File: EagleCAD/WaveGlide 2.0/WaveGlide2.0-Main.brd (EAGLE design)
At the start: 100 x 100 mm, 7 parts, among them K1 AQY21SOP, K2 MS-20-310-HN, U1 ATMEGA328P_TQFP, U2 BMP180, U3 MPXV7002, X1 22-23-2111

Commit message: Updated docs and part additions
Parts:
- added IC1: TPS77033, texas:SOT23-DBV
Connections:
- net GND: now also IC1.2
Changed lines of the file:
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@@
 <attribute name="OC_NEWARK" value="27C9916" x="15.7" y="94.9" size="1.778" layer="27" display="off"/>
+</element>
+<element name="IC1" library="texas" library_urn="urn:adsk.eagle:library:387" package="SOT23-DBV" value="TPS77033" x="26.5" y="49">
+<attribute name="MF" value="TEXAS INSTRUMENTS" x="26.5" y="49" size="1.778" layer="27" display="off"/>
+<attribute name="MPN" value="TPS77033DBVT" x="26.5" y="49" size="1.778" layer="27" display="off"/>
+<attribute name="OC_FARNELL" value="8461570" x="26.5" y="49" size="1.778" layer="27" display="off"/>
+<attribute name="OC_NEWARK" value="77C1187" x="26.5" y="49" size="1.778" layer="27" display="off"/>
 </element>
 </elements>
@@
 <signal name="GND">
 <contactref element="U2" pad="7"/>
+<contactref element="K2" pad="P$3"/>
+<contactref element="IC1" pad="2"/>
 <contactref element="U3" pad="3"/>
-<contactref element="K2" pad="P$3"/>
-<wire x1="59.482" y1="89.18" x2="11.48" y2="41.97" width="0" layer="19" extent="1-1"/>
-<wire x1="49.4" y1="25.45" x2="59.482" y2="89.18" width="0" layer="19" extent="1-1"/>
+<wire x1="26.5" y1="47.7" x2="59.482" y2="89.18" width="0" layer="19" extent="1-1"/>
+<wire x1="11.48" y1="41.97" x2="26.5" y2="47.7" width="0" layer="19" extent="1-1"/>
+<wire x1="49.4" y1="25.45" x2="26.5" y2="47.7" width="0" layer="19" extent="1-1"/>
 </signal>
 <signal name="VDD">

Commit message: Updated Schematic
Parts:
- removed X1: 22-23-2111, con-molex:22-23-2111
- added C10, C6: 10uF/16V, microbuilder:_0805MP
- added C7, C8: 1.0uF, microbuilder:_0805MP
- added C9: 10uF, microbuilder:_0805MP
- added D4, D5: 1N4148, microbuilder:SOD-323
- added R1: 560k, microbuilder:_0805MP
- added R2: 50, microbuilder:_0805MP
- added U5: UG-2828GDEDF11, microbuilder:FPC_XF2M-3015-1A
- IC1: device texas:SOT23-DBV -> CustomParts:SOT23-DBV
- U1: device SparkFun-IC-Microcontroller:TQFP32-08 -> CustomParts:TQFP32-08
- U2: device SparkFun-Sensors:BMP180 -> CustomParts:BMP180
- moved IC1 56.2 mm to (-5.00, 2.50)
- moved D1 14.0 mm to (19.9, 27.4)
- moved U1 13.5 mm to (13.5, 69.5)
- moved U3 9.61 mm to (42.0, 81.0)
- moved U2 9.54 mm to (9.50, 51.5)
- moved K2 9.43 mm to (40.0, 31.0)
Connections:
- new net 13V: C6.1, U5.P$29
- new net 3V3: C7.1, C9.1, U5.P$27, U5.P$4
- new net N$2: D4.A, R2.1
- new net N$3: C10.1, U5.P$28
- new net N$4: U5.P$5
- new net N$5: D4.C, D5.A
- new net N$6: C8.1
- new net N$7: R1.2, U5.P$9
- new net N$8: R2.2, U5.P$26
- new net OLED_BS0: U5.P$14
- new net OLED_CS: U5.P$12
- new net OLED_DC: U5.P$11
- new net OLED_MOSI: U5.P$18
- new net OLED_RES: U5.P$10
- new net OLED_SCK: U5.P$17
- net GND: now also C10.2, C6.2, C7.2, C8.2, C9.2, D5.C, K2.3, R1.1, U5.P$1, U5.P$13, U5.P$3, U5.P$30; no longer K2.P$3
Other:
- board size 100 x 100 mm -> 79 x 103 mm

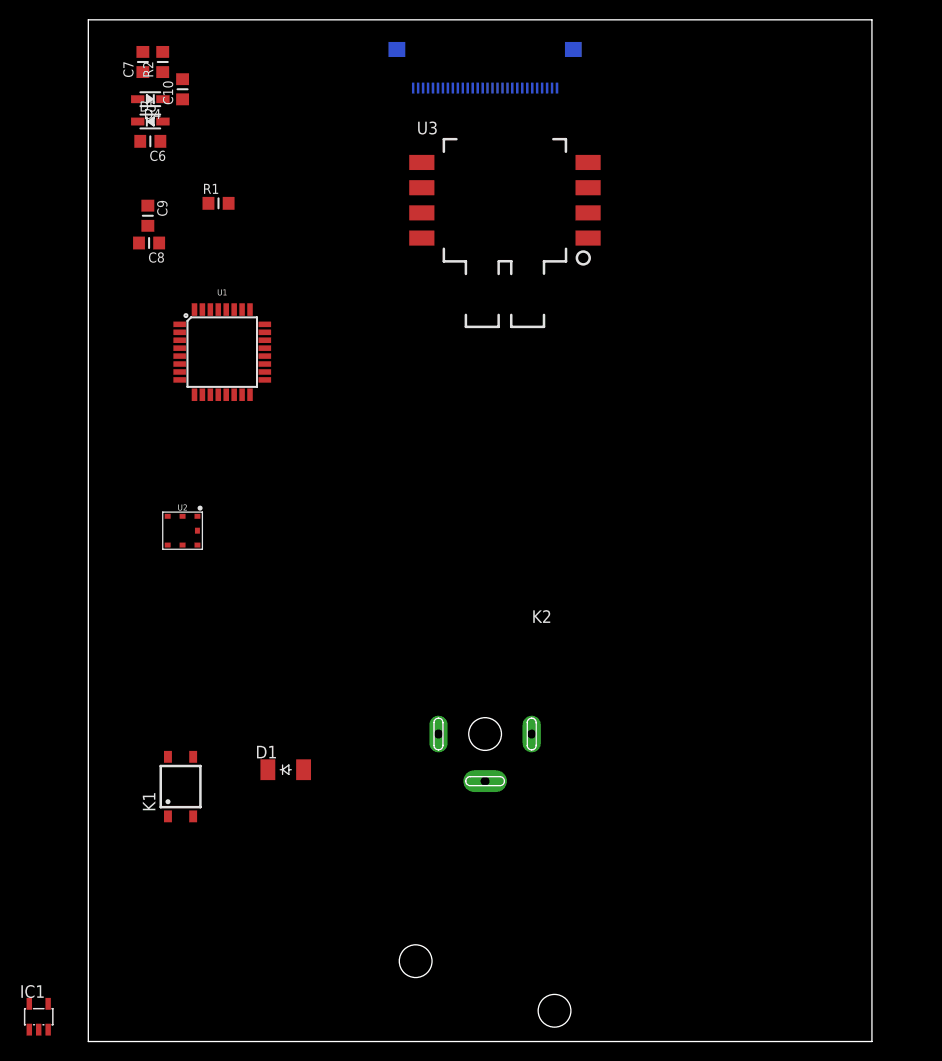
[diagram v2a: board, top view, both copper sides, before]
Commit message: Start generating schematic
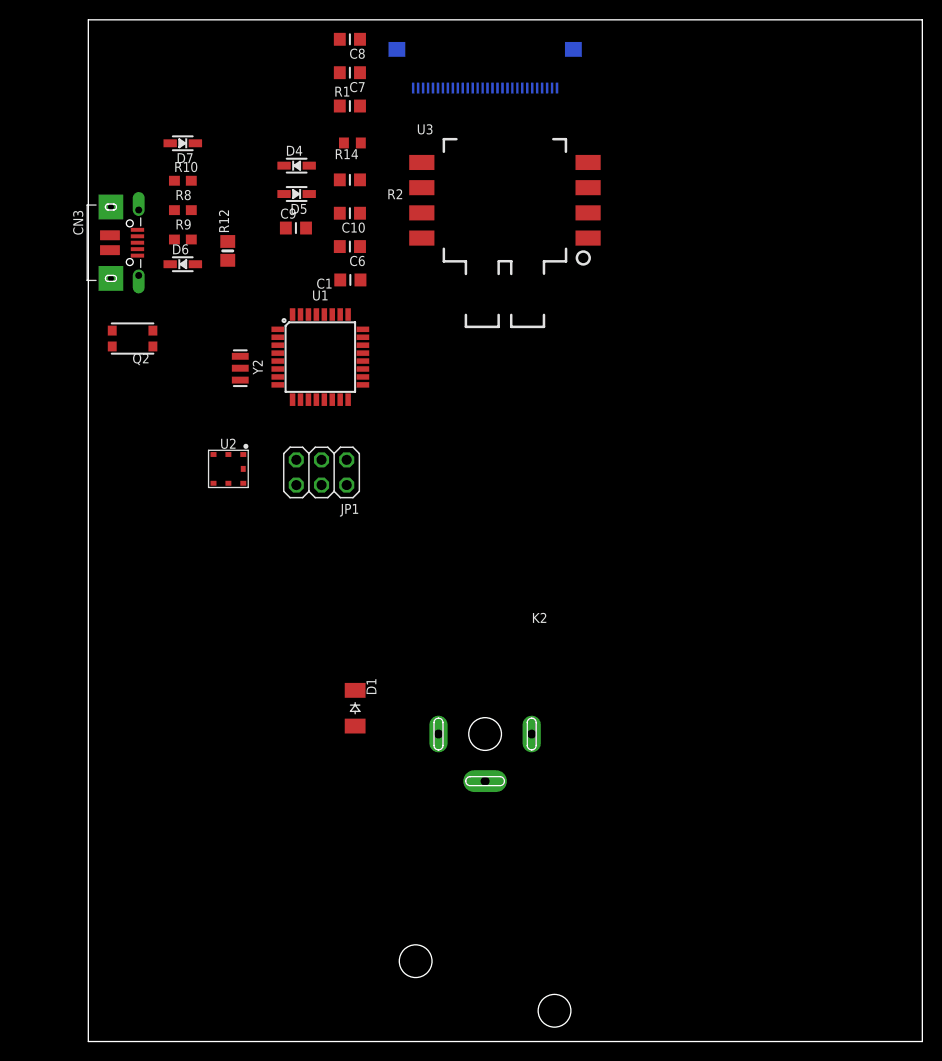
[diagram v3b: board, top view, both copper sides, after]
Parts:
- removed IC1: TPS77033, CustomParts:SOT23-DBV
- removed K1: AQY21SOP, relay:SOP04
- added C1: 0.1uF, microbuilder:_0805MP
- added CN3: 0, microbuilder:4UCONN_20329
- added D6: 3.6v, microbuilder:SOD-323
- added D7: 3.6V, microbuilder:SOD-323
- added JP1: 0, pinhead:2X03
- added Q2: reset, microbuilder:BTN_KMR2_4.6X2.8
- added R10: 1.5K (0603), microbuilder:0603-NO
- added R12: 10K, microbuilder:0805-NO
- added R14: 10k, resistor:R0603
- added R8, R9: 68 (0603), microbuilder:0603-NO
- added Y2: 12MHz, SparkFun:RESONATOR-SMD
- moved C8 28.8 mm to (26.4, 101.0)
- moved C6 22.7 mm to (26.4, 80.1)
- moved R2 22.3 mm to (26.4, 86.9), turned to 180 degrees
- moved C10 21.0 mm to (26.4, 83.5), turned to 180 degrees
- moved C7 20.9 mm to (26.4, 97.7), turned to 180 degrees
- moved R1 16.5 mm to (26.4, 94.3)
- moved D5 16.5 mm to (21.0, 85.4), turned to 180 degrees
- moved D4 16.2 mm to (21.0, 88.3), turned to 0 degrees
- moved C9 15.0 mm to (20.9, 82.0), turned to 0 degrees
- moved U1 9.90 mm to (23.4, 69.0)
- moved D1 9.35 mm to (26.9, 33.6), turned to 270 degrees
- moved U2 7.76 mm to (14.1, 57.7)
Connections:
- net 13V renamed SYS_13V
- net N$3 renamed OLED_VCOMH
- net N$7 renamed OLED_IREF
- net N$8 renamed OLED_VSL
- removed net 3V3: C7.1, C9.1, U5.P$27, U5.P$4
- removed net N$4: U5.P$5
- removed net N$6: C8.1
- removed net OLED_BS0: U5.P$14
- removed net OLED_CS: U5.P$12
- removed net OLED_DC: U5.P$11
- removed net OLED_MOSI: U5.P$18
- removed net OLED_RES: U5.P$10
- removed net OLED_SCK: U5.P$17
- removed net VDD: U2.2
- removed net VDDIO: U2.3
- new net BMP180_3V3: U2.2, U2.3
- new net D+1: CN3.D+, D6.C, R9.1
- new net D-1: CN3.D-, D7.C, R10.1, R8.1
- new net MCU_AREF: C1.1, U1.20
- new net MCU_I2C_SCL: U1.28, U2.5
- new net MCU_I2C_SDA: U1.27, U2.6
- new net MCU_OLED_CS: R14.1, U1.14, U5.P$12
- new net MCU_OLED_DC: U1.12, U5.P$11
- new net MCU_OLED_RES: U1.13, U5.P$10
- new net MCU_PROG/OLED_MOSI: JP1.4, U1.15, U5.P$18
- new net MCU_PROG/OLED_SCK: JP1.3, U1.17, U5.P$17
- new net MCU_PROG_MISO: JP1.1, U1.16
- new net MCU_RESET: JP1.5, Q2.A, Q2.A', R12.1, U1.29
- new net MPXV_5V: U3.2
- new net MPXV_VS: U1.26, U3.4
- new net N$10: U1.8, Y2.3
- new net N$9: U1.7, Y2.1
- new net OLED_VDD: C8.1, U5.P$5
- new net SOLENOID_12V: D1.C, K2.1
- new net SYS_3V3: C7.1, C9.1, R10.2, R12.2, R14.2, U1.18, U1.4, U1.6, U5.P$27, U5.P$4
- new net USB_D+: R9.2, U1.32
- new net USB_D-: R8.2, U1.11
- new net VBUS: CN3.VBUS
- net GND: now also C1.2, CN3.BASE@1, CN3.BASE@2, CN3.GND, CN3.SPRT@1, CN3.SPRT@2, CN3.SPRT@3, CN3.SPRT@4, D1.A, D6.A, D7.A, JP1.6, K2.2, Q2.B, Q2.B', U1.21, U1.3, U1.5, U5.P$14, U5.P$15, U5.P$16, U5.P$20, U5.P$21, U5.P$22, U5.P$23, U5.P$24, Y2.2; no longer IC1.2
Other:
- board size 79 x 103 mm -> 84.1 x 103 mm

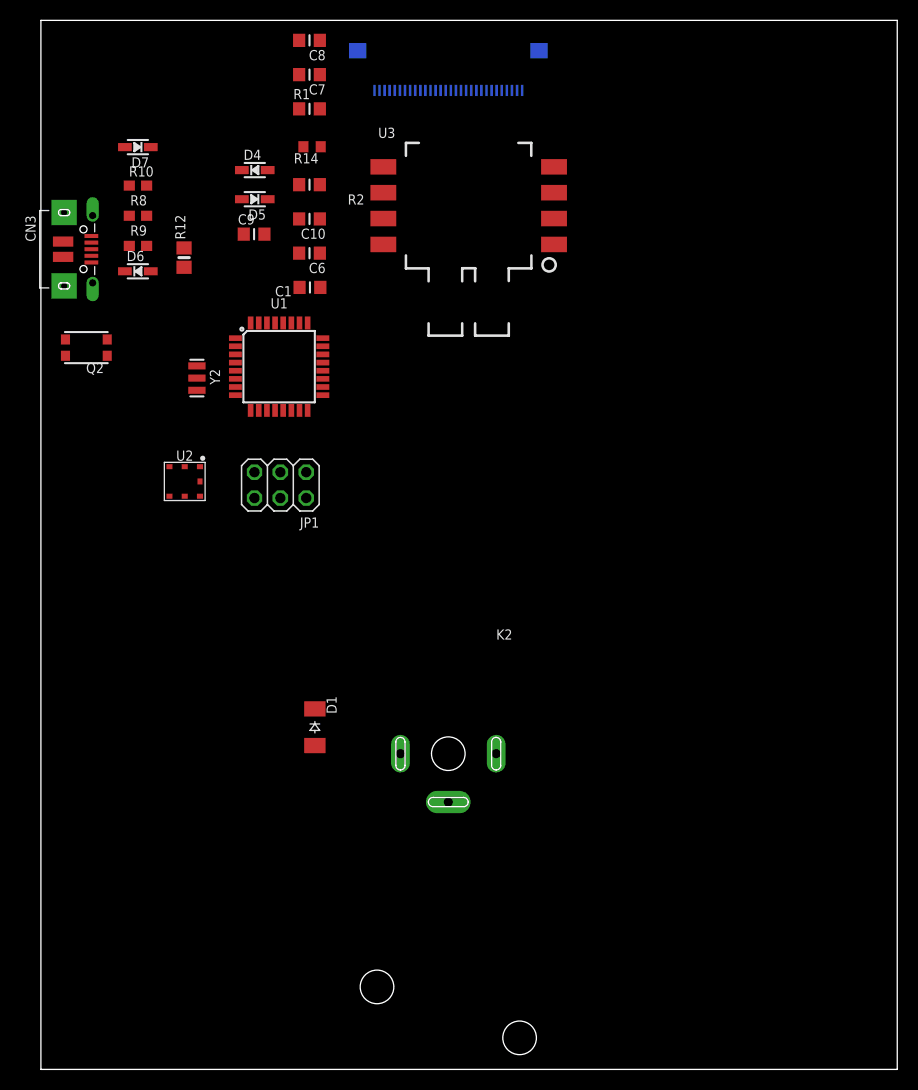
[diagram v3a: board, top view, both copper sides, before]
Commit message: Add buffer divider network, and floorplanning
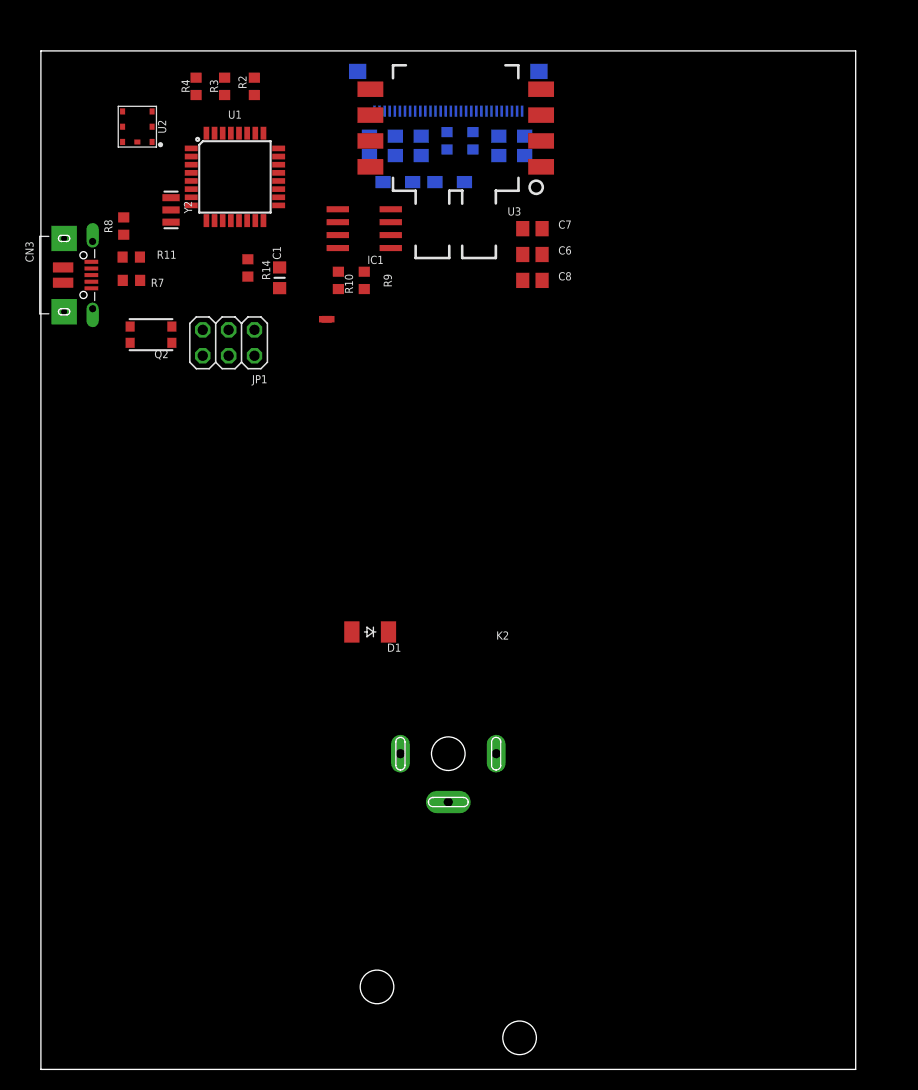
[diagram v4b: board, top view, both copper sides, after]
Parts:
- removed C10: 10uF/16V, microbuilder:_0805MP
- removed C9: 10uF, microbuilder:_0805MP
- removed D4, D5: 1N4148, microbuilder:SOD-323
- removed D6: 3.6v, microbuilder:SOD-323
- removed D7: 3.6V, microbuilder:SOD-323
- removed R12: 10K, microbuilder:0805-NO
- added C11, C3, C5: 10uF, resistor:C0805
- added C2, C4: 1.0uF, resistor:C0805
- added D2, D3: 1N4148, diode:SOD323-W
- added IC1: MC33502D, linear:SO08
- added R11, R7: 68, resistor:R0603
- added R3, R4: 10k, resistor:R0603
- added R6: 50, resistor:R0603
- added U$2: SHORT, CustomParts:SHORT
- C6: value 10uF/16V -> 0.01uF; device microbuilder:_0805MP -> resistor:C0805
- C7: device microbuilder:_0805MP -> resistor:C0805
- C8: value 1.0uF -> 470pF; device microbuilder:_0805MP -> resistor:C0805
- R1: device microbuilder:_0805MP -> resistor:R0603
- R10: value 1.5K (0603) -> 3.3k; device microbuilder:0603-NO -> resistor:R0603
- R2: value 50 -> 10k; device microbuilder:_0805MP -> resistor:R0603
- R8: value 68 (0603) -> 1.5k; device microbuilder:0603-NO -> resistor:R0603
- R9: value 68 (0603) -> 1.7k; device microbuilder:0603-NO -> resistor:R0603
- moved U2 35.1 mm to (9.47, 92.6), turned to 270 degrees
- moved C8 32.2 mm to (48.3, 77.5), turned to 0 degrees
- moved C7 26.6 mm to (48.3, 82.5), turned to 0 degrees
- moved R9 22.5 mm to (31.8, 77.5), turned to 270 degrees
- moved C6 21.9 mm to (48.3, 80.0), turned to 0 degrees
- moved R10 21.8 mm to (29.2, 77.5), turned to 270 degrees
- moved U1 19.1 mm to (19.1, 87.6)
- moved Y2 16.7 mm to (12.8, 84.4)
- moved JP1 14.9 mm to (18.4, 71.3)
- moved R1 13.9 mm to (39.9, 91.2), flipped to the bottom, turned to 90 degrees
- moved R14 13.5 mm to (20.3, 78.7), turned to 270 degrees
- moved U3 11.5 mm to (40.7, 92.4)
- moved R2 11.1 mm to (21.0, 96.5), turned to 90 degrees
- moved D1 10.8 mm to (32.3, 43.0), turned to 180 degrees
- moved Q2 6.48 mm to (10.8, 72.1)
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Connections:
- removed net BMP180_3V3: U2.2, U2.3
- removed net MPXV_5V: U3.2
- removed net MPXV_VS: U1.26, U3.4
- removed net N$5: D4.C, D5.A
- new net AGND: C6.2, C7.2, C8.2, IC1.4, R10.2, U$2.P$2, U3.3
- new net BUF1_LOOP: IC1.1, IC1.2, R9.1
- new net MPXV_VS_5V: C8.1, IC1.3, U3.4
- new net MPXV_VS_MCU: IC1.6, IC1.7, U1.26
- new net N$1: D2.C, D3.A
- new net N$4: IC1.5, R10.1, R9.2
- new net SYS_5V: C6.1, C7.1, IC1.8, U3.2
- net D+1: now also R7.2; no longer D6.C, R9.1
- net D-1: now also R11.2, R8.2; no longer D7.C, R10.1, R8.1
- net GND: now also C11.2, C2.2, C3.2, C4.2, C5.2, D3.C, U$2.P$1; no longer C10.2, C6.2, C7.2, C8.2, C9.2, D5.C, D6.A, D7.A, U3.3
- net MCU_I2C_SCL: now also R3.1
- net MCU_I2C_SDA: now also R4.1
- net MCU_RESET: now also R2.1; no longer R12.1
- net N$2: now also D2.A, R6.1; no longer D4.A, R2.1
- net OLED_VCOMH: now also C5.1; no longer C10.1
- net OLED_VDD: now also C2.1; no longer C8.1
- net OLED_VSL: now also R6.2; no longer R2.2
- net SYS_13V: now also C11.1; no longer C6.1
- net SYS_3V3: now also C3.1, C4.1, R2.2, R3.2, R4.2, R8.1, U2.2, U2.3; no longer C7.1, C9.1, R10.2, R12.2
- net USB_D+: now also R7.1; no longer R9.2
- net USB_D-: now also R11.1; no longer R8.2
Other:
- board size 84.1 x 103 mm -> 80 x 100 mm

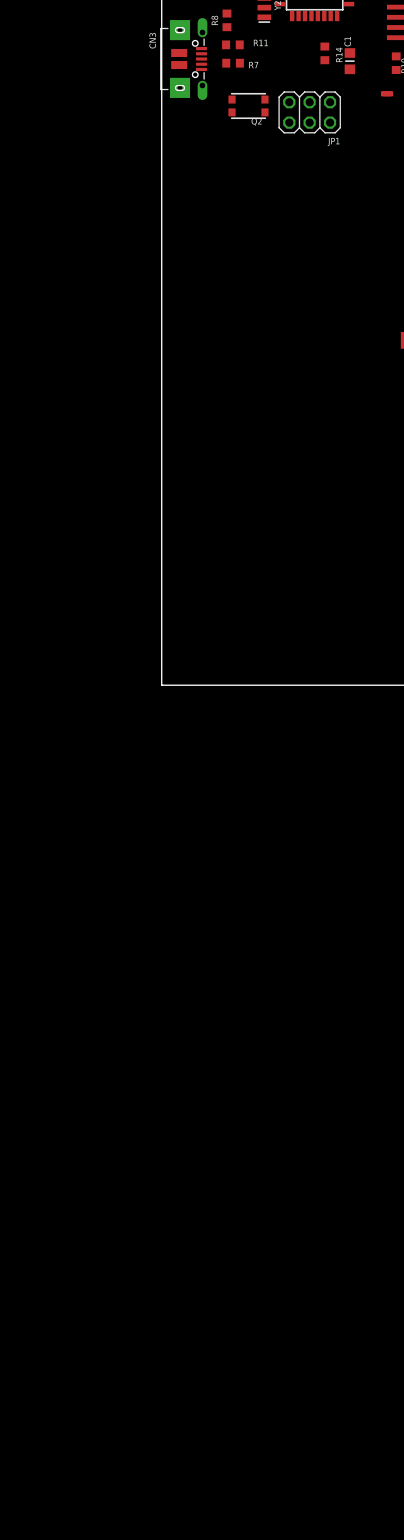
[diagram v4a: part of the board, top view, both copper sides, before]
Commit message: Add TPS55340 boost circuit
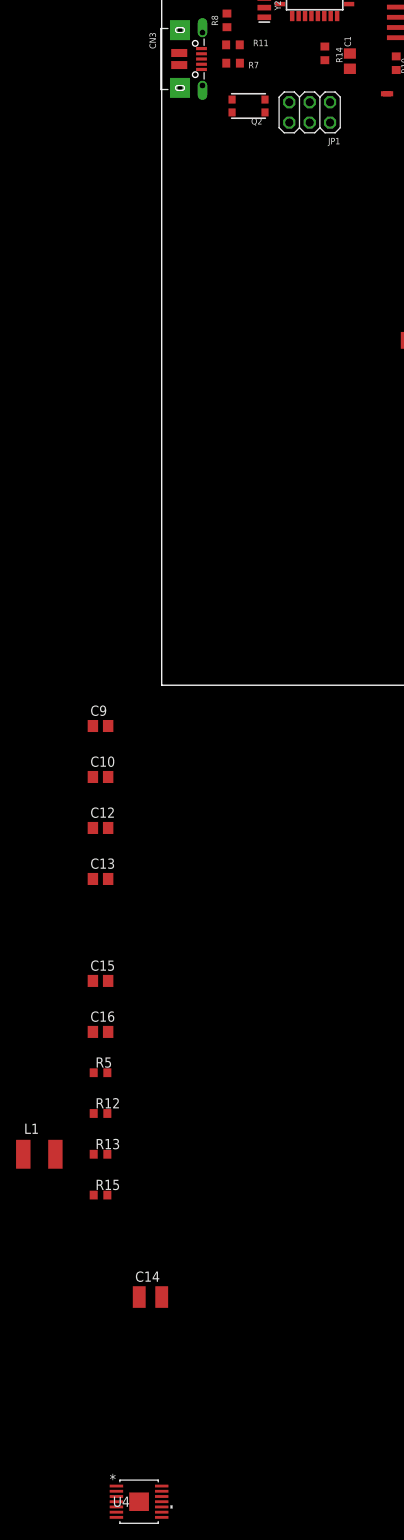
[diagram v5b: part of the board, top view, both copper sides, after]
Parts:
- added C10, C16: 100nF, resistor:C0805
- added C12: 22nF, resistor:C0805
- added C13: 10nF, resistor:C0805
- added C14: 22uF, resistor:C1210
- added C15: 1.0uF, resistor:C0805
- added C9: 10uF, resistor:C0805
- added L1: 3.3uH, resistor:L4532P
- added R12: 953, resistor:R0603
- added R13: 86.6k, resistor:R0603
- added R15: 10k, resistor:R0603
- added R5: 60.4k, resistor:R0603
- added U4: TPS55340PWP, CustomParts:PWP14
- C1: device microbuilder:_0805MP -> resistor:C0805
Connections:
- new net SOLENOID_EN: U4.4
- new net TPS55340_COMP: C13.1, R12.2, U4.8
- new net TPS55340_FB: R13.2, R15.1, U4.9
- new net TPS55340_FREQ: R5.2, U4.10
- new net TPS55340_SS: C12.1, U4.5
- new net TPS55340_SW: L1.1, U4.1, U4.2
- new net TPS66340_COMP1: C16.1, R12.1
- new net VBAT: C10.1, C9.1, L1.2, U4.3
- net GND: now also C10.2, C12.2, C13.2, C14.2, C15.2, C16.2, C9.2, R15.2, R5.1, U4.12, U4.13, U4.14, U4.15, U4.7
- net SOLENOID_12V: now also C14.1, C15.1, R13.1
